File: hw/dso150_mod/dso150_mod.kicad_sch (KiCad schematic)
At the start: 5 parts, among them J1 USB4085-GF-A, J2 Conn_01x02

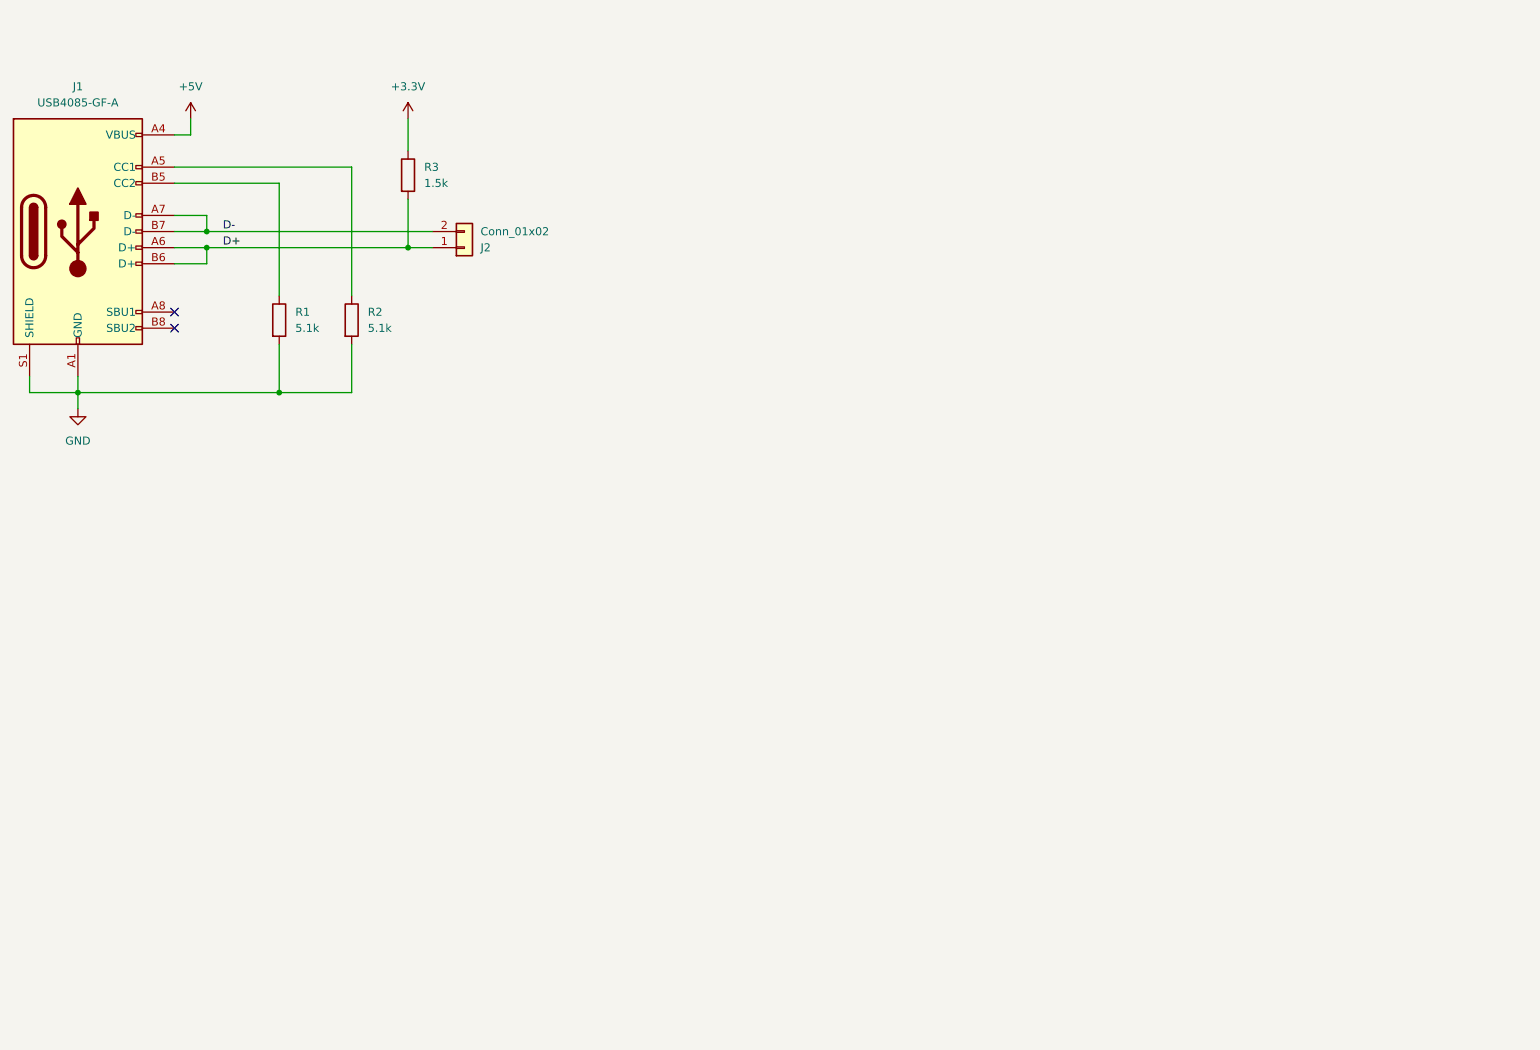
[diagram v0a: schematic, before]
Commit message: Start on kicad 9 redesign
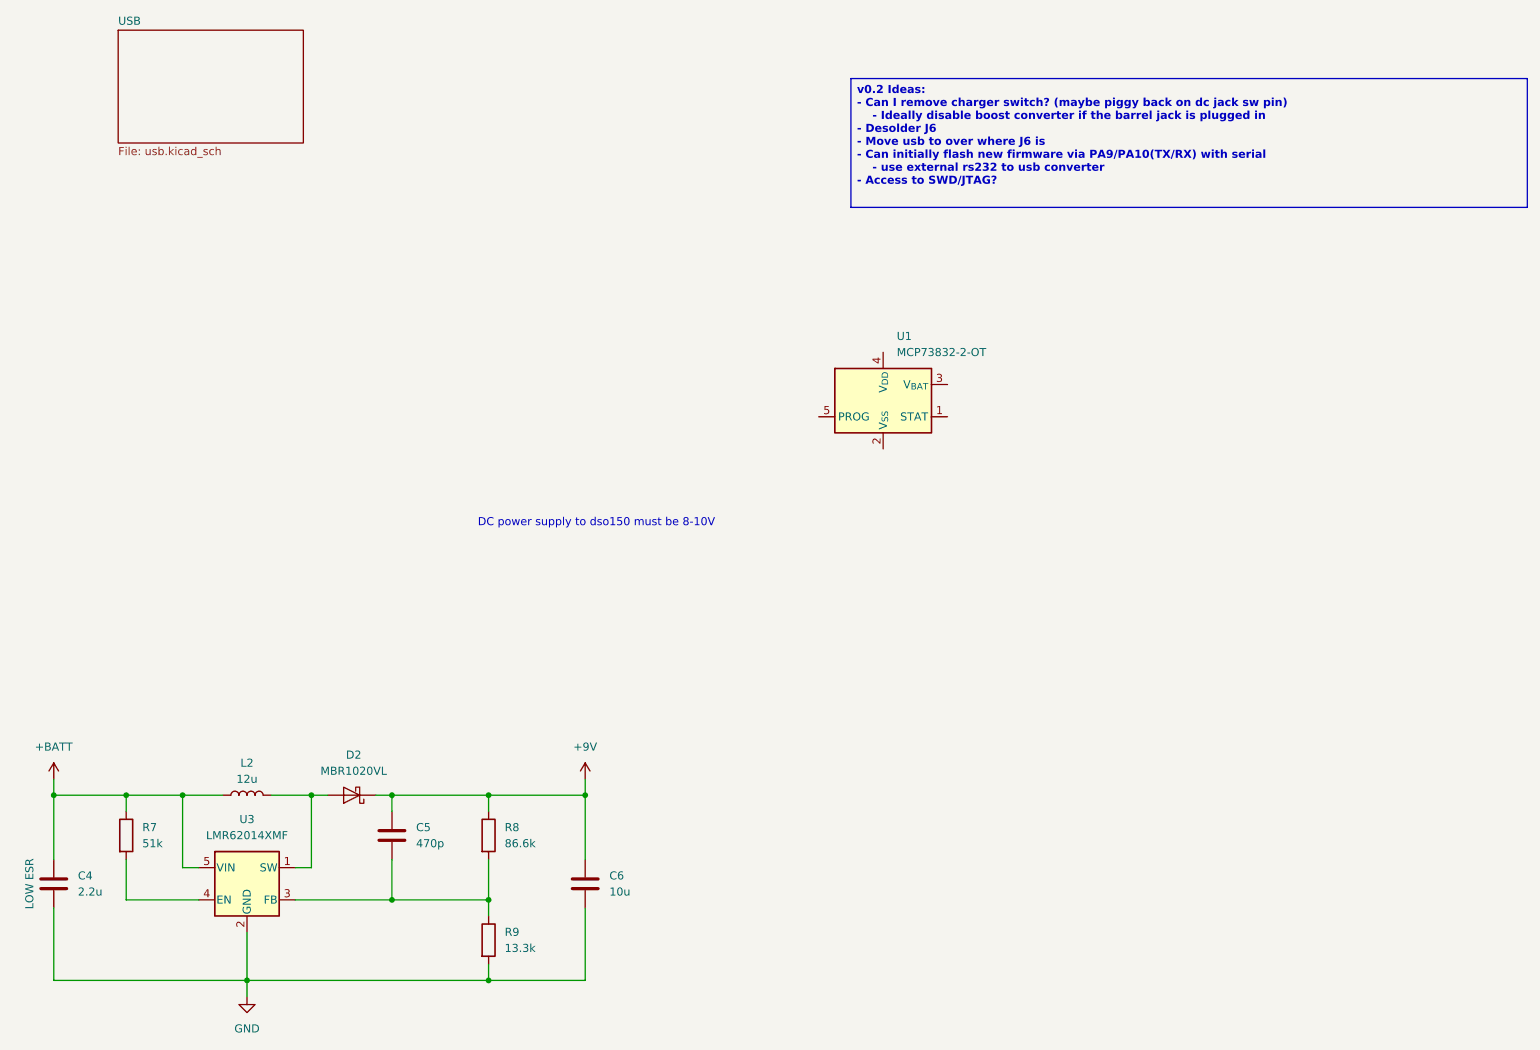
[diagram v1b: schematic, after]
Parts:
- removed J1: USB4085-GF-A, symbol Connector:USB_C_Receptacle_USB2.0_16P
- removed J2: Conn_01x02, symbol Connector_Generic:Conn_01x02
- removed R1, R2: 5.1k, symbol Device:R
- removed R3: 1.5k, symbol Device:R
- added C4: 2.2u, symbol Device:C
- added C5: 470p, symbol Device:C
- added C6: 10u, symbol Device:C
- added D2: MBR1020VL, Diode_SMD:D_SOD-123F, symbol Diode:MBR1020VL
- added L2: 12u, symbol Device:L
- added R7: 51k, symbol Device:R
- added R8: 86.6k, symbol Device:R
- added R9: 13.3k, symbol Device:R
- added U1: MCP73832-2-OT, Package_TO_SOT_SMD:SOT-23-5, symbol Battery_Management:MCP73832-2-OT
- added U3: LMR62014XMF, Package_TO_SOT_SMD:SOT-23-5, symbol Regulator_Switching:LMR62014XMF
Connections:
- net GND: now also C4.2, C6.2, R9.2, U3.2 (GND)
- new net: R7.2, U3.4 (EN)
- new net: C5.2, R8.2, R9.1, U3.3 (FB)
- new net: D2.2 (A), L2.2, U3.1 (SW)
- new net +9V: C5.1, C6.1, D2.1 (K), R8.1
- new net +BATT: C4.1, L2.1, R7.1, U3.5 (VIN)
- no-connect marks 2 -> 0
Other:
- added sheet USB (usb.kicad_sch)
- note added: "DC power supply to dso150 must be 8-10V"
